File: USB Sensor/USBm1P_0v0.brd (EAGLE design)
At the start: 33 x 20 mm, 17 parts, among them J1 USB_MICRO, J2 CONN_42.54_SCREW, U1 PAC1710

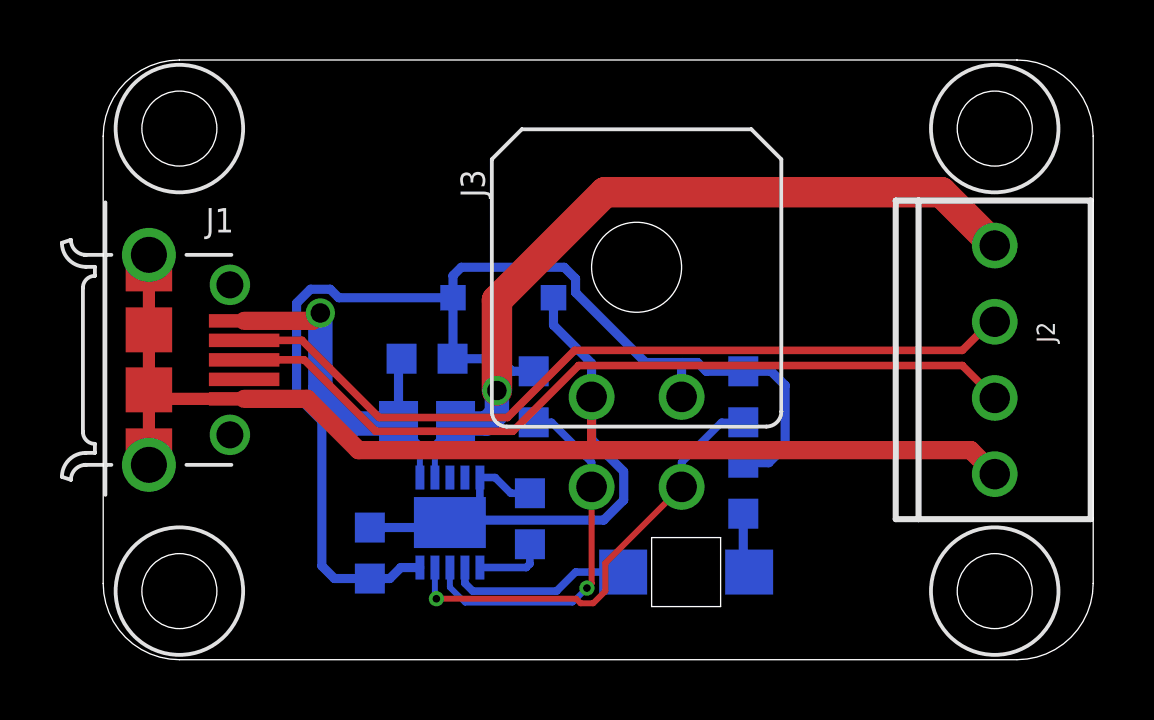
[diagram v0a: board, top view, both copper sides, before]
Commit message: Minor cleanup for USBA1P and USBm1P
Cleanup to part naming and layout for A1P and micro setups
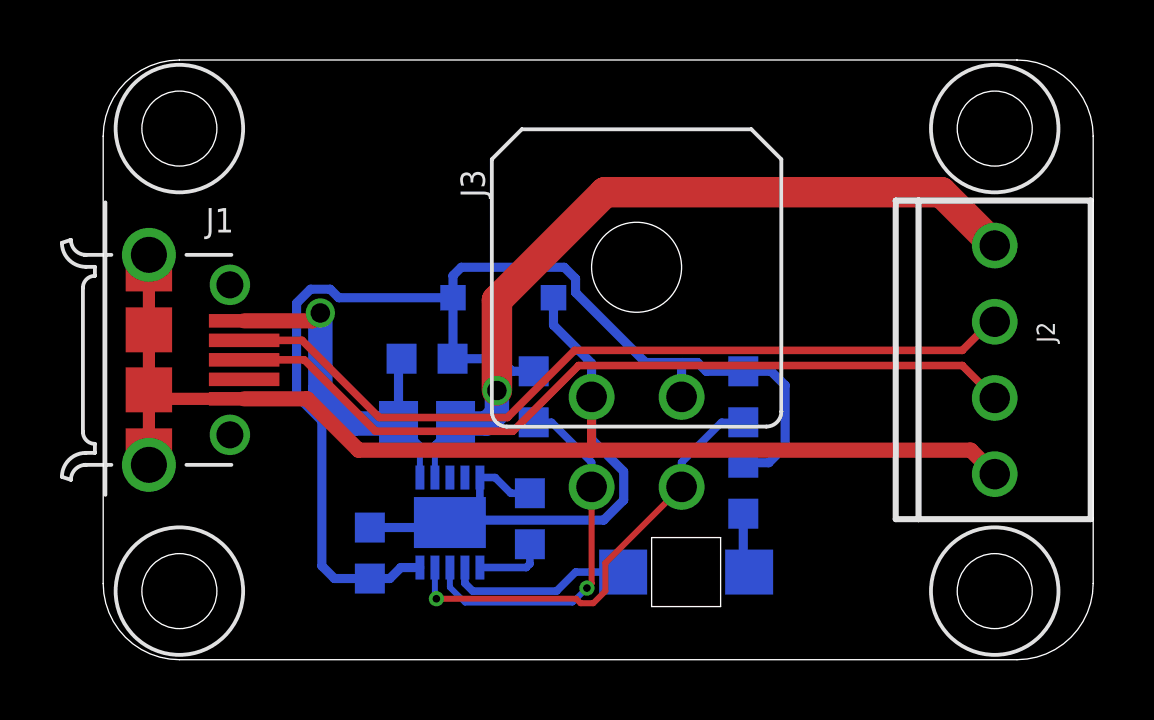
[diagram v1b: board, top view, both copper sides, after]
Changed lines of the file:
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@@
 <contactref element="J1" pad="5"/>
 <contactref element="J2" pad="4"/>
-<wire x1="4.699" y1="8.695" x2="6.799" y2="8.695" width="0.6096" layer="1"/>
-<wire x1="28.918" y1="6.985" x2="29.718" y2="6.185" width="0.6096" layer="1"/>
-<wire x1="6.799" y1="8.695" x2="8.509" y2="6.985" width="0.6096" layer="1"/>
-<wire x1="8.509" y1="6.985" x2="16.256" y2="6.985" width="0.6096" layer="1"/>
-<wire x1="16.256" y1="6.985" x2="28.918" y2="6.985" width="0.6096" layer="1"/>
+<wire x1="4.699" y1="8.695" x2="6.799" y2="8.695" width="0.508" layer="1"/>
+<wire x1="28.918" y1="6.985" x2="29.718" y2="6.185" width="0.508" layer="1"/>
+<wire x1="6.799" y1="8.695" x2="8.509" y2="6.985" width="0.508" layer="1"/>
+<wire x1="8.509" y1="6.985" x2="16.256" y2="6.985" width="0.508" layer="1"/>
+<wire x1="16.256" y1="6.985" x2="28.918" y2="6.985" width="0.508" layer="1"/>
 <wire x1="16.28" y1="8.761" x2="16.28" y2="7.009" width="0.3048" layer="1"/>
 <wire x1="16.28" y1="7.009" x2="16.256" y2="6.985" width="0.3048" layer="1"/>
@@
 <wire x1="10.557" y1="7.162" x2="9.845" y2="7.874" width="0.2" layer="16"/>
 <contactref element="J1" pad="1"/>
-<wire x1="4.699" y1="11.295" x2="6.977" y2="11.295" width="0.6096" layer="1"/>
-<wire x1="6.977" y1="11.295" x2="7.239" y2="11.557" width="0.6096" layer="1"/>
+<wire x1="4.699" y1="11.295" x2="6.977" y2="11.295" width="0.508" layer="1"/>
+<wire x1="6.977" y1="11.295" x2="7.239" y2="11.557" width="0.508" layer="1"/>
 </signal>
 <signal name="USB_LOAD">
